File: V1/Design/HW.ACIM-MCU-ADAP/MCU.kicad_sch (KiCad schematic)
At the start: 28 parts, among them J101 HEADER 2x15POS, J102 HEADER 2x15POS, U101 MIPS 32-bit DSC, U102 12MHz

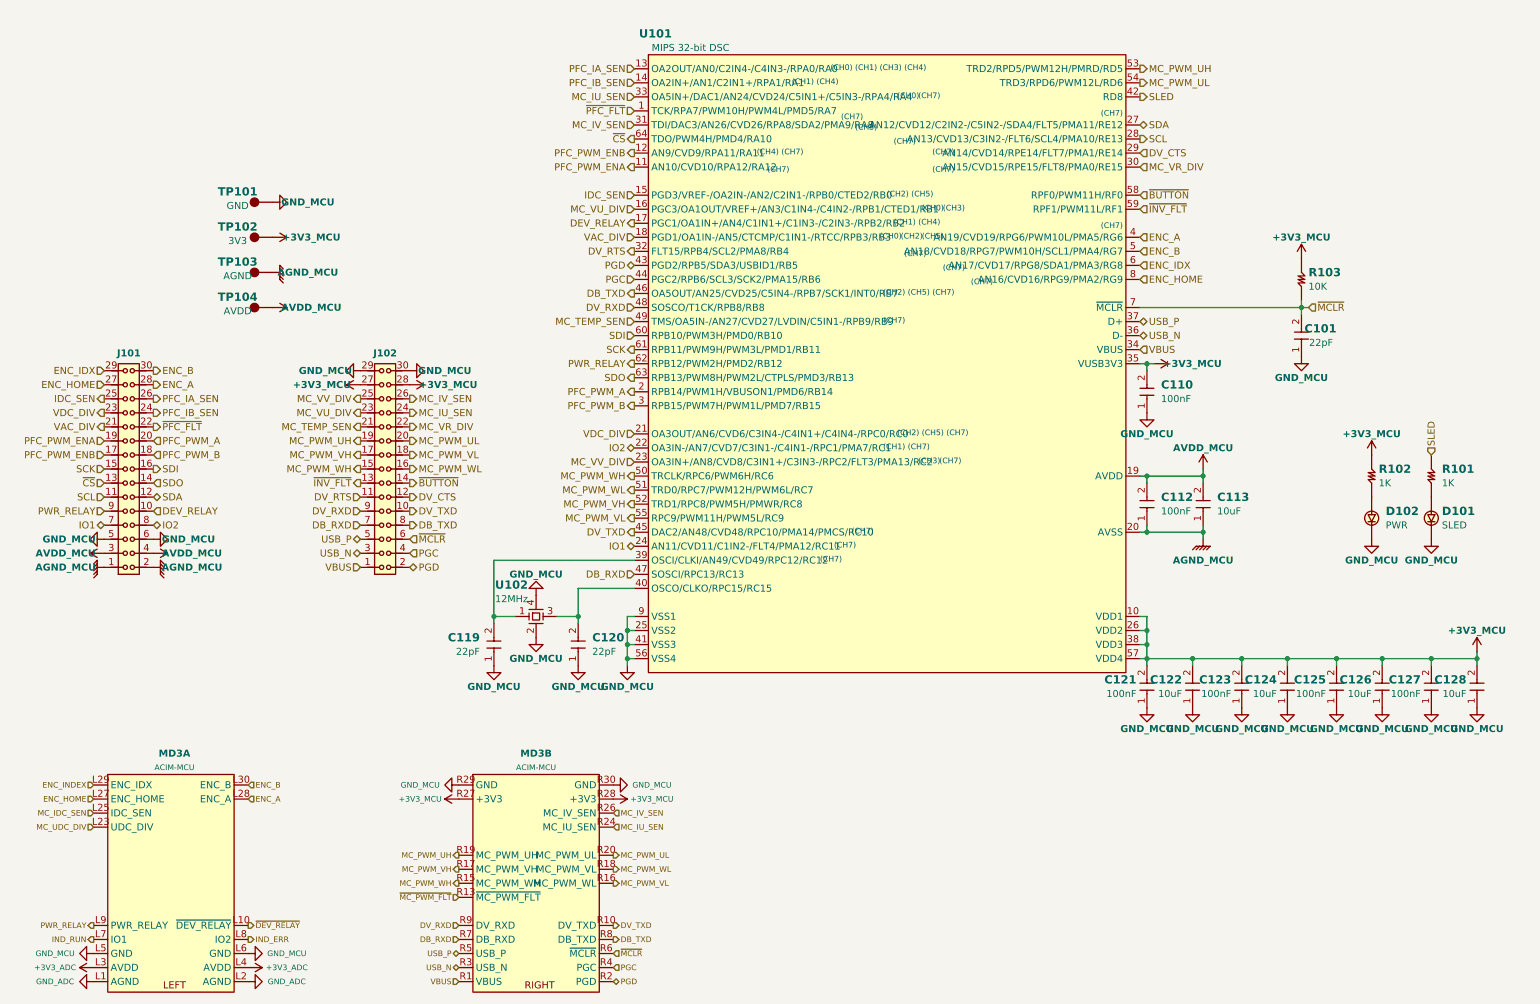
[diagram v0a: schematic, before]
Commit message: HW.ACIM-MCU-ADAP schematic update 1
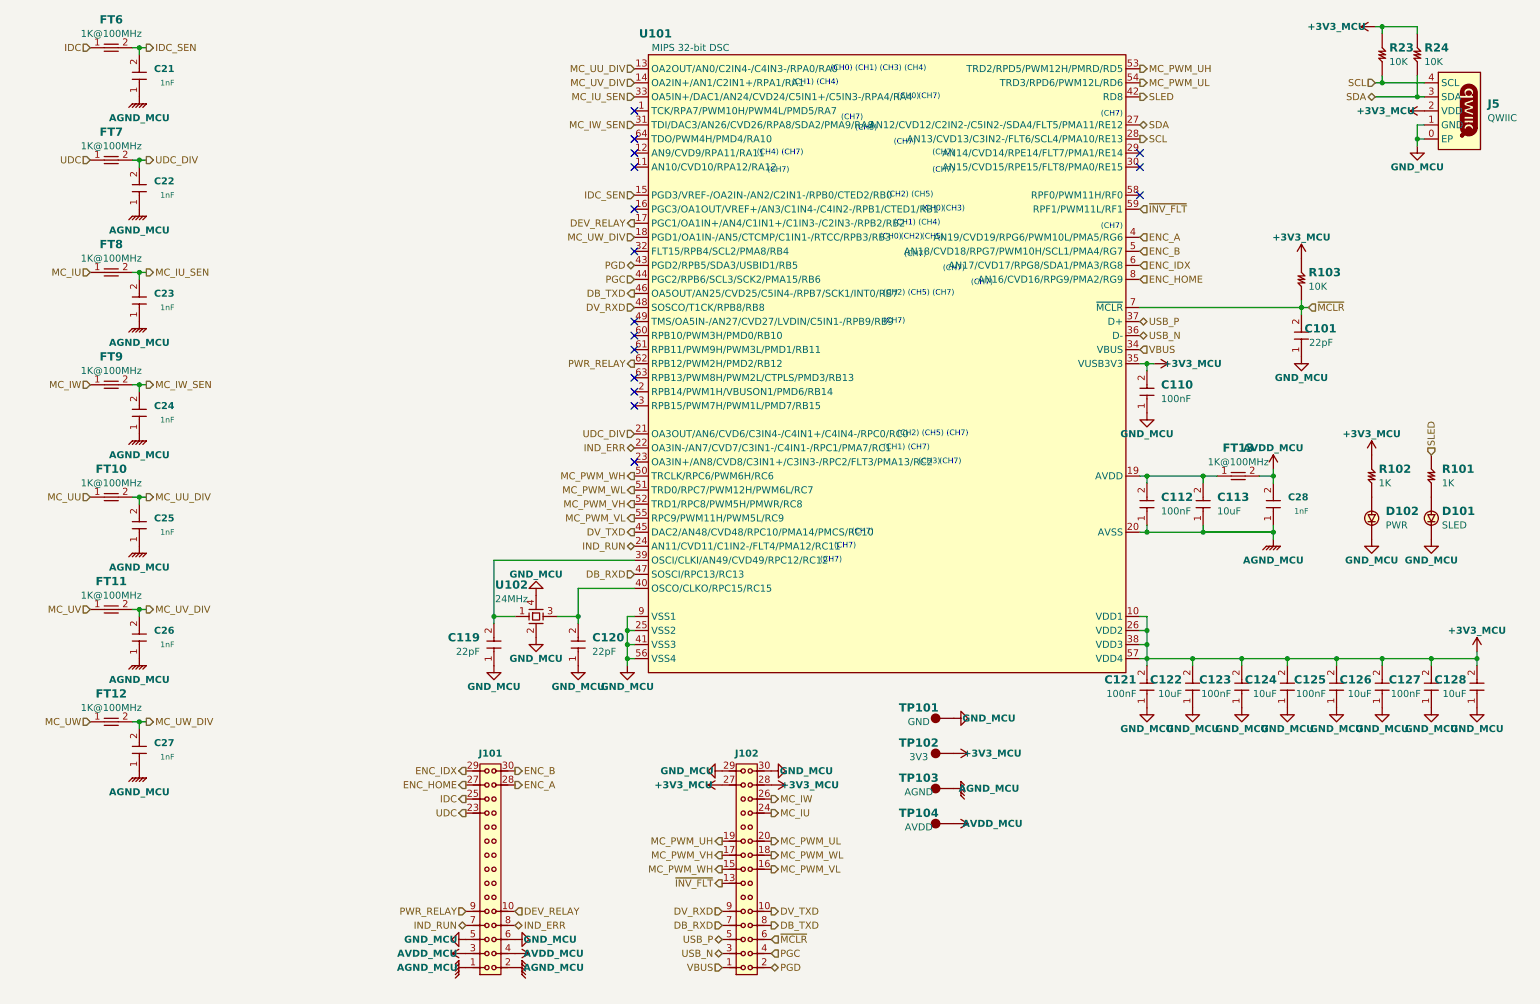
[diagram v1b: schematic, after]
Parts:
- removed MD3: ACIM-MCU, SAMPI:HW.ACIM-MCU_SMD, symbol SAMPI:HW.ACIM-MCU
- added C21, C22, C23, C24, C25, C26, C27: 1nF, SAMPI:CAP0402, symbol SAMPI:CERCAP
- added C28: 1nF, SAMPI:CAP0603, symbol SAMPI:CERCAP
- added FT10, FT11, FT12, FT13, FT6, FT7, FT8, FT9: 1K@100MHz, SAMPI:IND0402, symbol SAMPI:FerriteBead
- added J5: QWIIC, SAMPI:HDM-1x4x1.0-RA, symbol SAMPI:QWIIC
- added R23, R24: 10K, SAMPI:RES0402, symbol SAMPI:RES
- U102: value 12MHz -> 24MHz
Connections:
- net IO1 is gone; now on net IND_RUN: J101.7, U101.24 (AN11/CVD11/C1IN2-/FLT4/PMA12/RC11)
- net IO2 is gone; now on net IND_ERR: J101.8, U101.22 (OA3IN-/AN7/CVD7/C3IN1-/C4IN1-/RPC1/PMA7/RC1)
- net +3V3_MCU: now also J5.2 (VDD), R23.2, R24.2
- net AGND_MCU: now also C21.1, C22.1, C23.1, C24.1, C25.1, C26.1, C27.1, C28.1
- net AVDD_MCU: now also C28.2, FT13.2; no longer C112.2, C113.2, U101.19 (AVDD)
- net GND_MCU: now also J5.0 (EP), J5.1 (GND)
- net IDC_SEN: now also C21.2, FT6.2; no longer J101.25
- net MC_IU_SEN: now also C23.2, FT8.2; no longer J102.24
- net MC_PWM_VL: now also J102.16; no longer J102.18
- net MC_PWM_WL: now also J102.18; no longer J102.16
- net SCL: now also J5.4 (SCL), R23.1; no longer J101.11
- net SDA: now also J5.3 (SDA), R24.1; no longer J101.12
- net DV_CTS: no longer names the net of U101.29 (AN14/CVD14/RPE14/FLT7/PMA1/RE14)
- net DV_CTS: no longer J102.12
- net DV_RTS: no longer names the net of U101.32 (FLT15/RPB4/SCL2/PMA8/RB4)
- net DV_RTS: no longer J102.11
- net MC_IV_SEN renamed MC_IW
- net MC_IW: now also FT9.1; no longer U101.31 (TDI/DAC3/AN26/CVD26/RPA8/SDA2/PMA9/RA8)
- net MC_TEMP_SEN: no longer names the net of U101.49 (TMS/OA5IN-/AN27/CVD27/LVDIN/C5IN1-/RPB9/RB9)
- net MC_TEMP_SEN: no longer J102.21
- net MC_VR_DIV: no longer names the net of U101.30 (AN15/CVD15/RPE15/FLT8/PMA0/RE15)
- net MC_VR_DIV: no longer J102.22
- net MC_VU_DIV: no longer names the net of U101.16 (PGC3/OA1OUT/VREF+/AN3/C1IN4-/C4IN2-/RPB1/CTED1/RB1)
- net MC_VU_DIV: no longer J102.23
- net MC_VV_DIV: no longer names the net of U101.23 (OA3IN+/AN8/CVD8/C3IN1+/C3IN3-/RPC2/FLT3/PMA13/RC2)
- net MC_VV_DIV: no longer J102.25
- net PFC_IA_SEN renamed MC_UU_DIV
- net MC_UU_DIV: now also C25.2, FT10.2; no longer J101.26
- net PFC_IB_SEN renamed MC_UV_DIV
- net MC_UV_DIV: now also C26.2, FT11.2; no longer J101.24
- net PFC_PWM_A: no longer names the net of U101.2 (RPB14/PWM1H/VBUSON1/PMD6/RB14)
- net PFC_PWM_A: no longer J101.20
- net PFC_PWM_B: no longer names the net of U101.3 (RPB15/PWM7H/PWM1L/PMD7/RB15)
- net PFC_PWM_B: no longer J101.18
- net PFC_PWM_ENA: no longer names the net of U101.11 (AN10/CVD10/RPA12/RA12)
- net PFC_PWM_ENA: no longer J101.19
- net PFC_PWM_ENB: no longer names the net of U101.12 (AN9/CVD9/RPA11/RA11)
- net PFC_PWM_ENB: no longer J101.17
- net SCK: no longer names the net of U101.61 (RPB11/PWM9H/PWM3L/PMD1/RB11)
- net SCK: no longer J101.15
- net SDI: no longer names the net of U101.60 (RPB10/PWM3H/PMD0/RB10)
- net SDI: no longer J101.16
- net SDO: no longer names the net of U101.63 (RPB13/PWM8H/PWM2L/CTPLS/PMD3/RB13)
- net SDO: no longer J101.14
- net VAC_DIV renamed MC_UW_DIV
- net MC_UW_DIV: now also C27.2, FT12.2; no longer J101.21
- net VDC_DIV renamed UDC
- net UDC: now also FT7.1; no longer U101.21 (OA3OUT/AN6/CVD6/C3IN4-/C4IN1+/C4IN4-/RPC0/RC0)
- net ~{BUTTON}: no longer names the net of U101.58 (RPF0/PWM11H/RF0)
- net ~{BUTTON}: no longer J102.14
- net ~{CS}: no longer names the net of U101.64 (TDO/PWM4H/PMD4/RA10)
- net ~{CS}: no longer J101.13
- net ~{PFC_FLT}: no longer names the net of U101.1 (TCK/RPA7/PWM10H/PWM4L/PMD5/RA7)
- net ~{PFC_FLT}: no longer J101.22
- new net: C112.2, C113.2, FT13.1, U101.19 (AVDD)
- new net IDC: FT6.1, J101.25
- new net MC_IU: FT8.1, J102.24
- new net MC_IW_SEN: C24.2, FT9.2, U101.31 (TDI/DAC3/AN26/CVD26/RPA8/SDA2/PMA9/RA8)
- new net MC_UU: FT10.1
- new net MC_UV: FT11.1
- new net MC_UW: FT12.1
- new net UDC_DIV: C22.2, FT7.2, U101.21 (OA3OUT/AN6/CVD6/C3IN4-/C4IN1+/C4IN4-/RPC0/RC0)
- no-connect marks 0 -> 16
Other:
- moved on the sheet: TP101, TP102, TP103, TP104

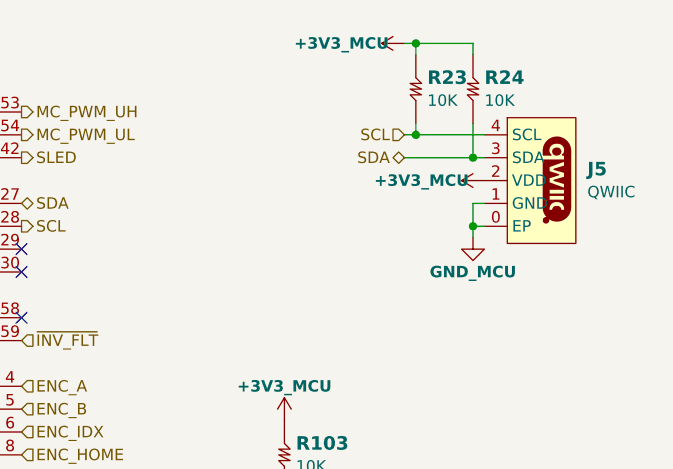
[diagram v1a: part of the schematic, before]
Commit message: HW.ACIM-MCU-ADAP schematic update 3
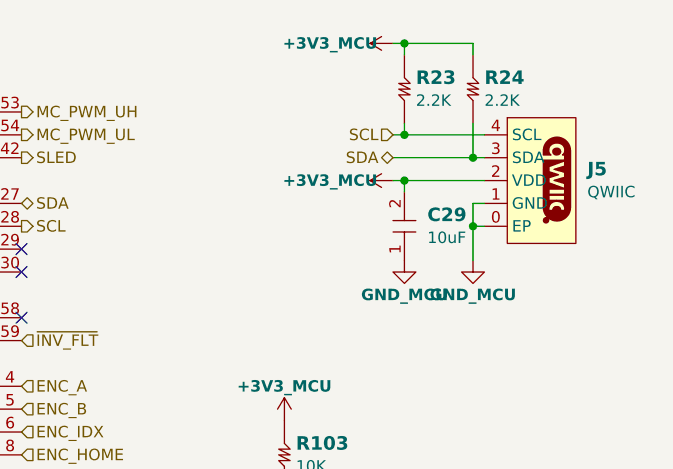
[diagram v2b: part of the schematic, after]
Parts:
- added C29: 10uF, SAMPI:CAP0402, symbol SAMPI:CERCAP
- C28: footprint SAMPI:CAP0603 -> SAMPI:CAP0402
- R23, R24: value 10K -> 2.2K
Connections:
- net +3V3_MCU: now also C29.2
- net GND_MCU: now also C29.1
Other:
- moved on the sheet: R23

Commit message: HW.ACIM-MCU-ADAP layout & production
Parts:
- C110, C112, C121, C123, C125, C127: MFT Murata -> Walsin; MNP GRM155R71H104ME14D -> 0402B104K500CT
- C113, C122, C124, C126, C128, C29: MFT Murata -> Samsung; MNP GRM155C80J106ME11D -> CL05A106MQ5NUNC
- C21, C22, C23, C24, C25, C26, C27, C28: MNP CL10B102KB8NNNC -> 0402B102K500CT
- FT10, FT11, FT12, FT13, FT6, FT7, FT8, FT9: MFT (none) -> TDK; MNP (none) -> BLM15AX102SN1D
- R23, R24: MNP RC0402JR-0710KL -> RC0402JR-072K2L

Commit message: HW.ACIM-MCU-ADAP_V0.0 update ibom
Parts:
- J5: MFT Amphenol ICC (FCI) -> Amphenol
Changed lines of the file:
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@@
 			)
 		)
-		(property "MFT" "Amphenol ICC (FCI)"
+		(property "MFT" "Amphenol"
 			(at 273.05 38.735 0)
 			(effects
